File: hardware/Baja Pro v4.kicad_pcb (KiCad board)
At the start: 2 copper layers, 73 x 65 mm, 29 parts, among them P1 Header-Female-2.54_1x4, P2 Header-Female-2.54_1x2, P4 Header-Female-2.54_1x6, U1 FM24CL04B-GTR_C365762, U2 DC-DC stepdown, U3 AMS1117-3.3, U4 Thermistor, X1 ESP32_WROOM32

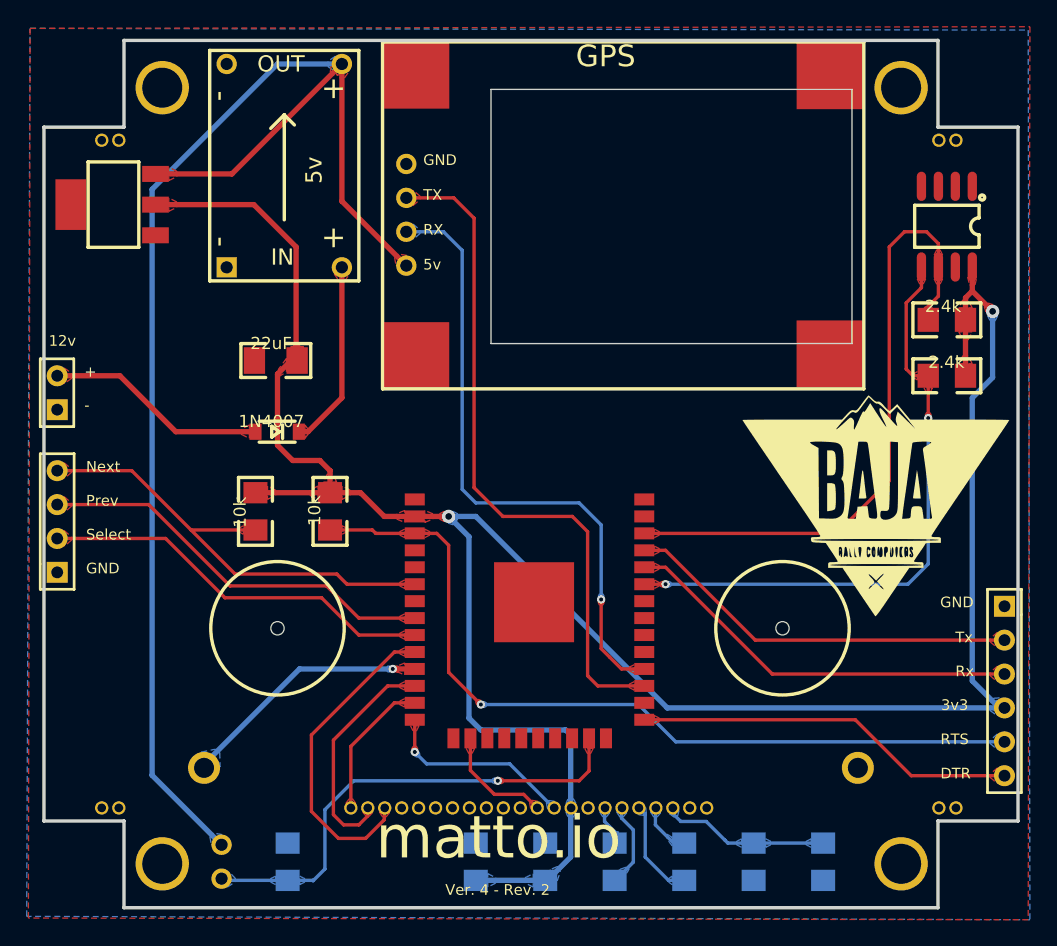
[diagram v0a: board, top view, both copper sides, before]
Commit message: Update to KiCAD9 Create missing symbols Replace symbols with KiCAD symbols Link symbols with footprints
Signed-off-by: Ilias Daradimos <judgedrid@gmail.com>
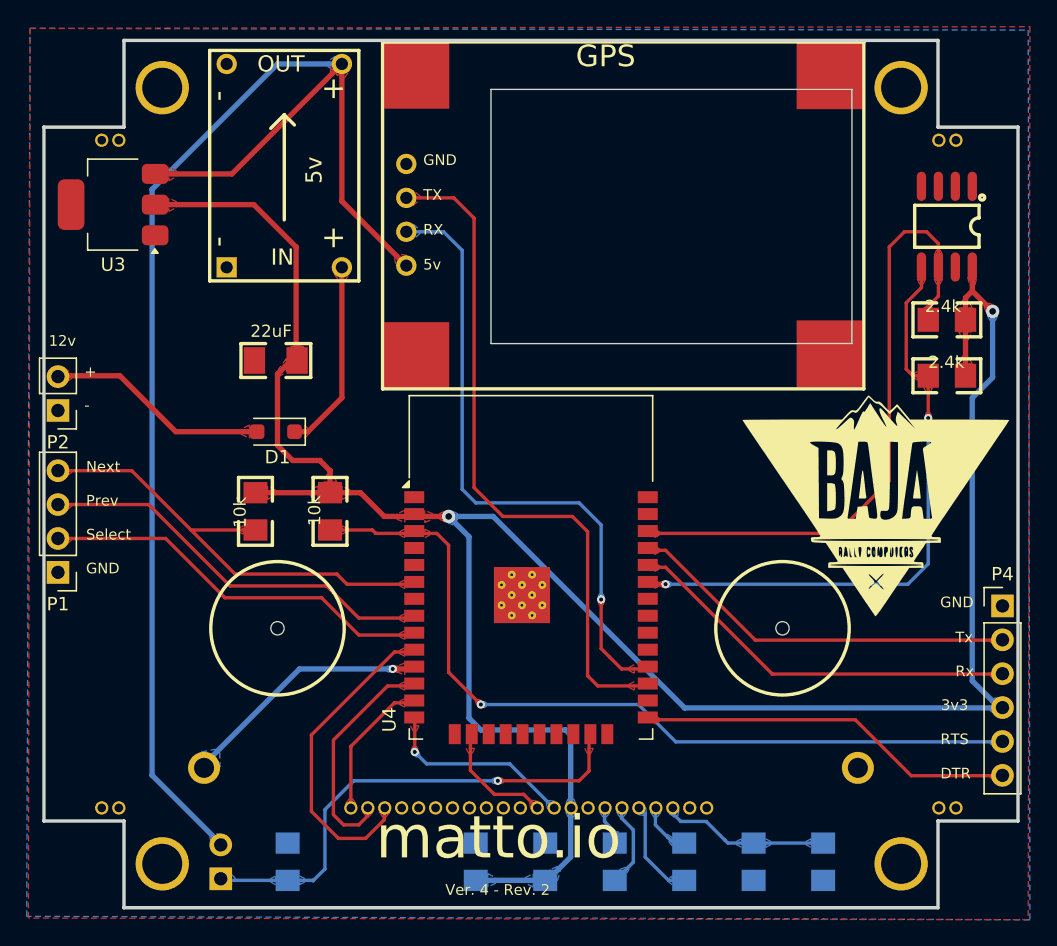
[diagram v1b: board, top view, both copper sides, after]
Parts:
- D1: footprint Baja Pro v4:SOD-123F -> Diode_SMD:D_SOD-123F
- J1: renamed from U4; footprint Baja Pro v4:THERMISTOR-PCB -> Connector_PinHeader_2.54mm:PinHeader_1x02_P2.54mm_Vertical
- P1: value Header-Female-2.54_1x4 -> Remote; footprint Baja Pro v4:HDR-4X1/2.54 -> Connector_PinHeader_2.54mm:PinHeader_1x04_P2.54mm_Vertical
- P2: value Header-Female-2.54_1x2 -> Power; footprint Baja Pro v4:HDR-1X2/2.54 -> Connector_PinHeader_2.54mm:PinHeader_1x02_P2.54mm_Vertical
- P4: value Header-Female-2.54_1x6 -> Flash; footprint Baja Pro v4:HDR-6X1/2.54 -> Connector_PinHeader_2.54mm:PinHeader_1x06_P2.54mm_Vertical
- U3: footprint Baja Pro v4:SOT-223 -> Package_TO_SOT_SMD:SOT-223-3_TabPin2
- U4: renamed from X1; value ESP32_WROOM32 -> ESP32-WROOM-32; footprint Baja Pro v4:WROOM32 -> RF_Module:ESP32-WROOM-32
- moved U4 11.9 mm to (146.7, 112.6)
- moved P4 6.38 mm to (182.0, 112.5), turned to 0 degrees
- moved P1 2.54 mm to (111.2, 110.0), turned to 180 degrees
- moved J1 1.28 mm to (123.4, 133.0), turned to 0 degrees
- moved P2 0.08 mm to (111.2, 97.9), turned to 180 degrees
- turned D1 to 180 degrees
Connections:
- net C1_1 renamed Net-(LCD1-VB0-)
- net C1_2 renamed Net-(LCD1-VB0+)
- net C2_1 renamed Net-(LCD1-VB1-)
- net C2_2 renamed Net-(LCD1-VB1+)
- net C3_2 renamed Net-(LCD1-VLCD)
- D1 pad 1: D1_1 -> Net-(D1-K)
- D1 pad 2: D1_2 -> Net-(D1-A)
- J1 pad 1: 5V -> TEMP
- J1 pad 2: TEMP -> 5V
- P2 pad 2: D1_1 -> Net-(D1-A)
- U1 pad 1: GND -> unconnected-(U1-NC-Pad1)
- U2 pad 2: D1_2 -> Net-(D1-K)
- U4 pad 17: X1_17 -> unconnected-(U4-SHD/SD2-Pad17)
- U4 pad 18: X1_18 -> unconnected-(U4-SWP/SD3-Pad18)
- U4 pad 19: X1_19 -> unconnected-(U4-SCS/CMD-Pad19)
- U4 pad 20: X1_20 -> unconnected-(U4-SCK/CLK-Pad20)
- U4 pad 21: X1_21 -> unconnected-(U4-SDO/SD0-Pad21)
- U4 pad 22: X1_22 -> unconnected-(U4-SDI/SD1-Pad22)
- U4 pad 24: X1_24 -> unconnected-(U4-IO2-Pad24)
- U4 pad 26: X1_26 -> unconnected-(U4-IO4-Pad26)
- U4 pad 29: X1_29 -> unconnected-(U4-IO5-Pad29)
- U4 pad 30: X1_30 -> unconnected-(U4-IO18-Pad30)
- U4 pad 31: X1_31 -> unconnected-(U4-IO19-Pad31)
- U4 pad 32: (no net) -> unconnected-(U4-NC-Pad32)
- U4 pad 37: X1_37 -> unconnected-(U4-IO23-Pad37)
- U4 pad 4: X1_4 -> unconnected-(U4-SENSOR_VP-Pad4)
- U4 pad 5: X1_5 -> unconnected-(U4-SENSOR_VN-Pad5)
- U4 pad 7: X1_7 -> unconnected-(U4-IO35-Pad7)
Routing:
- net Net-(D1-A): track 0.00 -> 16.2 mm
- net D1_1: track 16.2 -> 0.00 mm
- net Net-(D1-K): track 0.00 -> 14.1 mm
- net D1_2: track 14.1 -> 0.00 mm
- added copper zone on F.Cu, net Net-(D1-A)
- added copper zone on F.Cu, net Net-(D1-K)
- removed copper zone on F.Cu, net D1_1
- removed copper zone on F.Cu, net D1_2
